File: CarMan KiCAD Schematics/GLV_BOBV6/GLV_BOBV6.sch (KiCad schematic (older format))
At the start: 22 parts, among them J1 Conn_01x02, J2 Conn_01x02, J3 Conn_01x02, J4 Conn_02x02_Odd_Even, J5 Conn_02x02_Odd_Even, J6 J6, U1 INA226AIDGSR

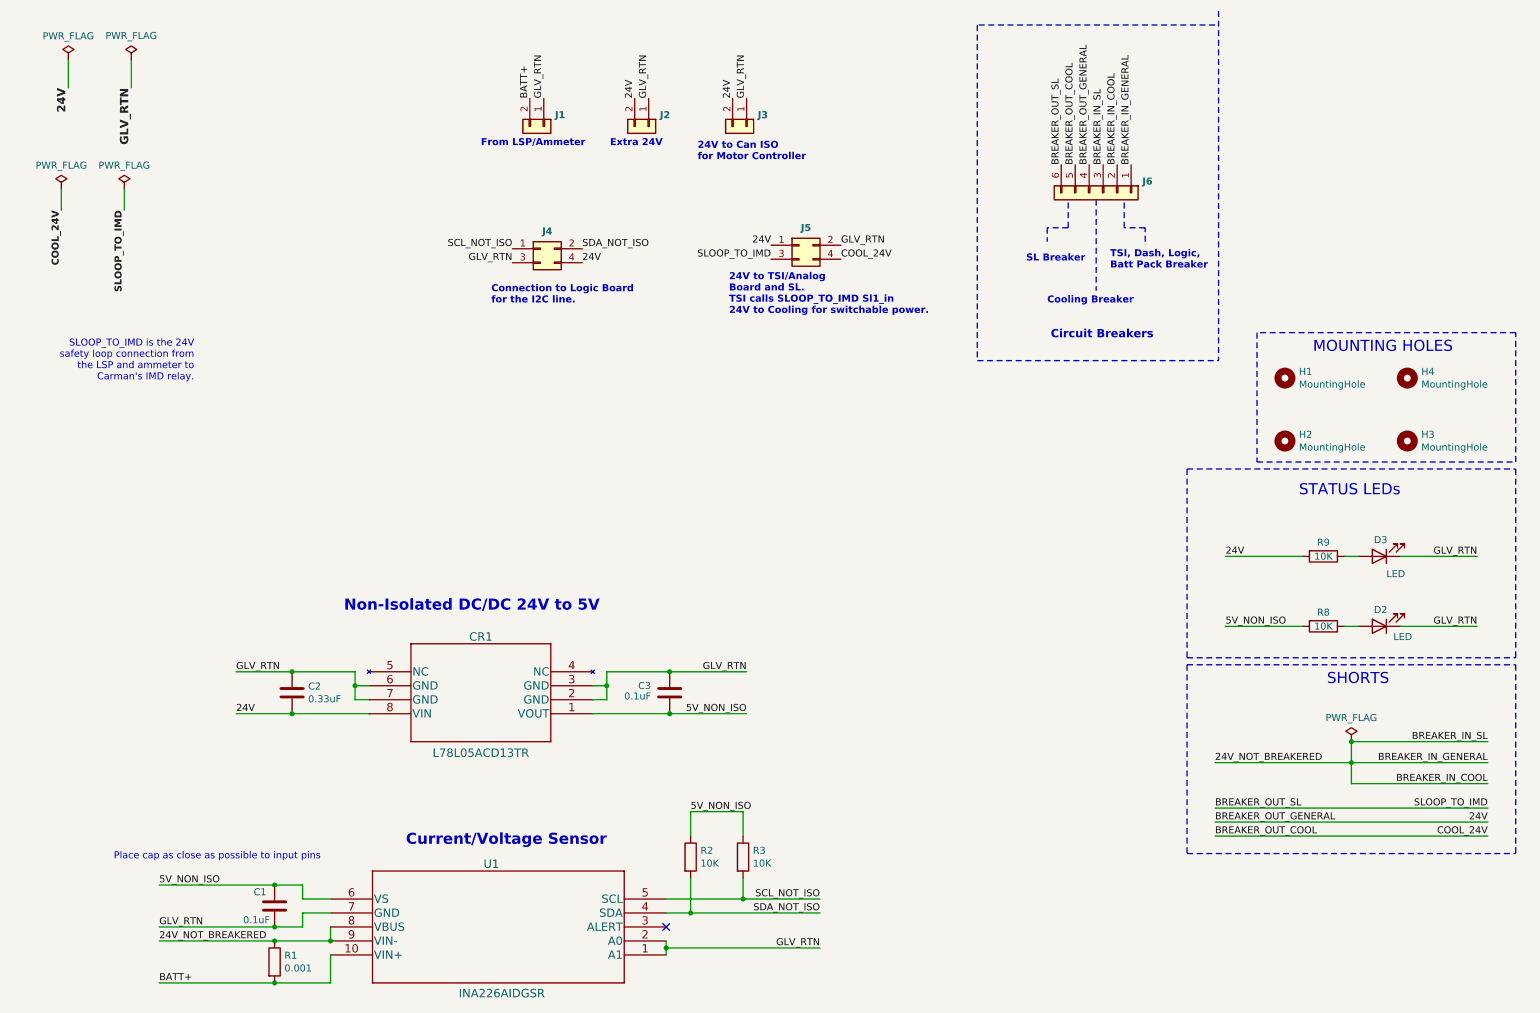
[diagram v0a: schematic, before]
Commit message: LOGIC: Added pull-up resistors on non-isolated side of I2C TSI:   Added silkscreen labeling and comments GLV:   Organized GLV schematic, increased mounting hole size to 3.5mm from 2.5mm
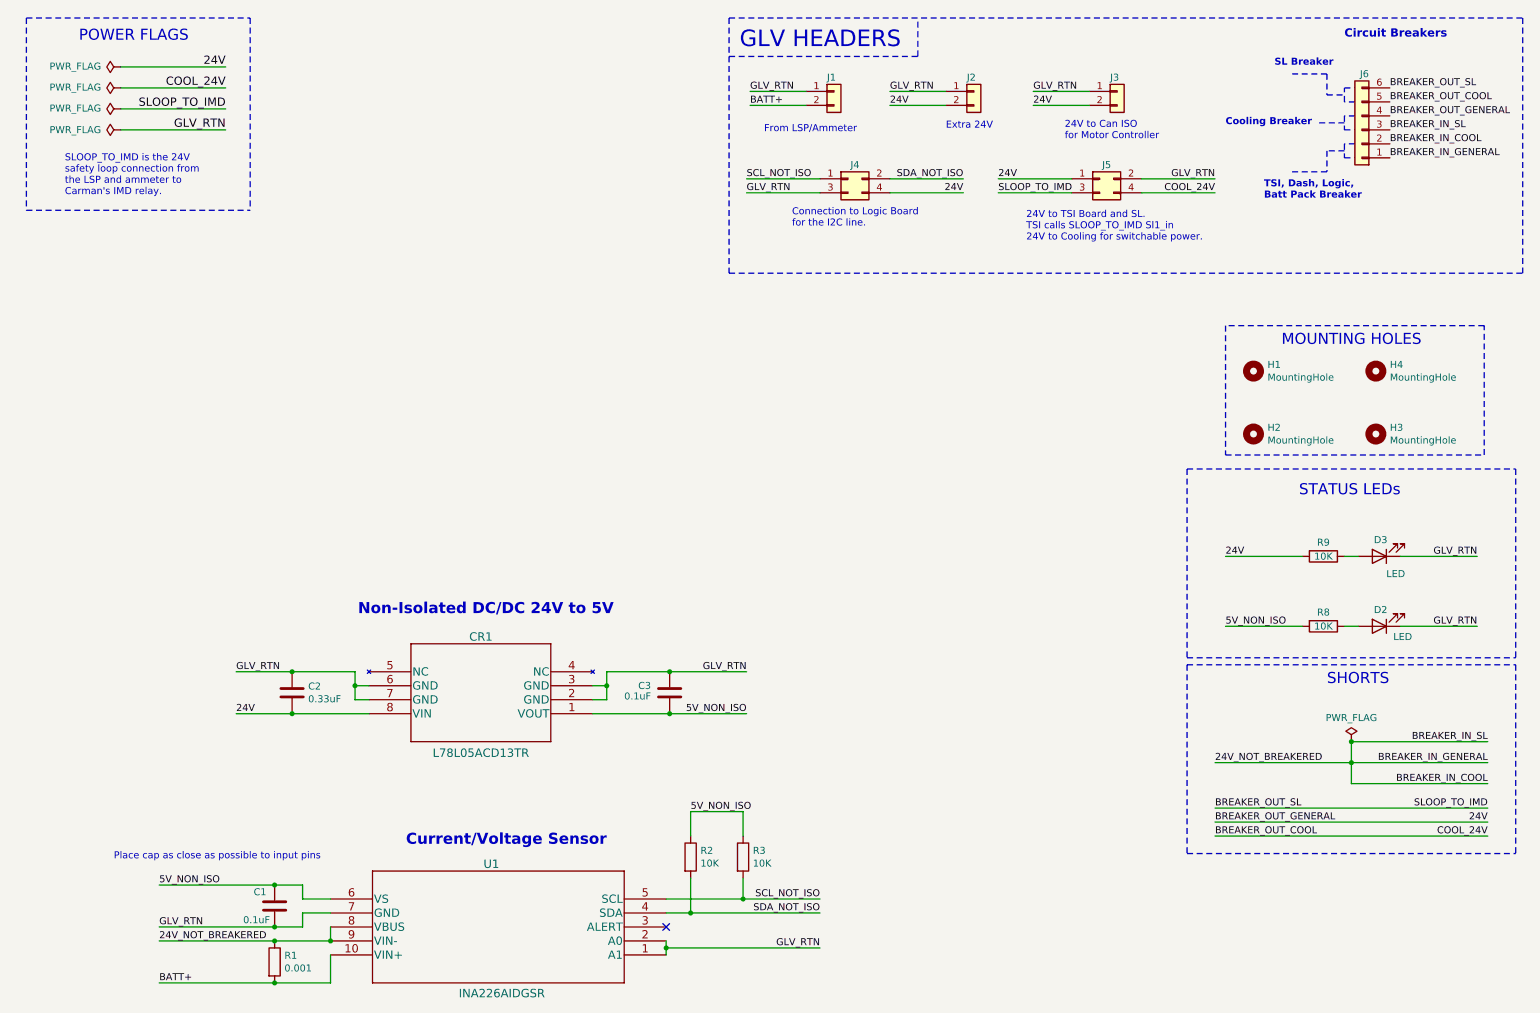
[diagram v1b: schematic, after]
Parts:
- H1, H2, H3, H4: footprint MountingHole:MountingHole_2.5mm_Pad -> MountingHole:MountingHole_3.5mm_Pad
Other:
- note added: "24V to TSI Board and SL. \nTSI calls SLOOP_TO_IMD Sl1_in\n24V to Cooling for switchable power."
- note added: "GLV HEADERS"
- note added: "POWER FLAGS"
- note removed: "24V to TSI/Analog\nBoard and SL. \nTSI calls SLOOP_TO_IMD Sl1_in\n24V to Cooling for switchable power."
- moved on the sheet: H1, H2, H3, H4, J1, J2, J3, J4, J5, J6
